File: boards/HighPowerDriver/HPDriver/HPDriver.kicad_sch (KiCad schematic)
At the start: 0 parts

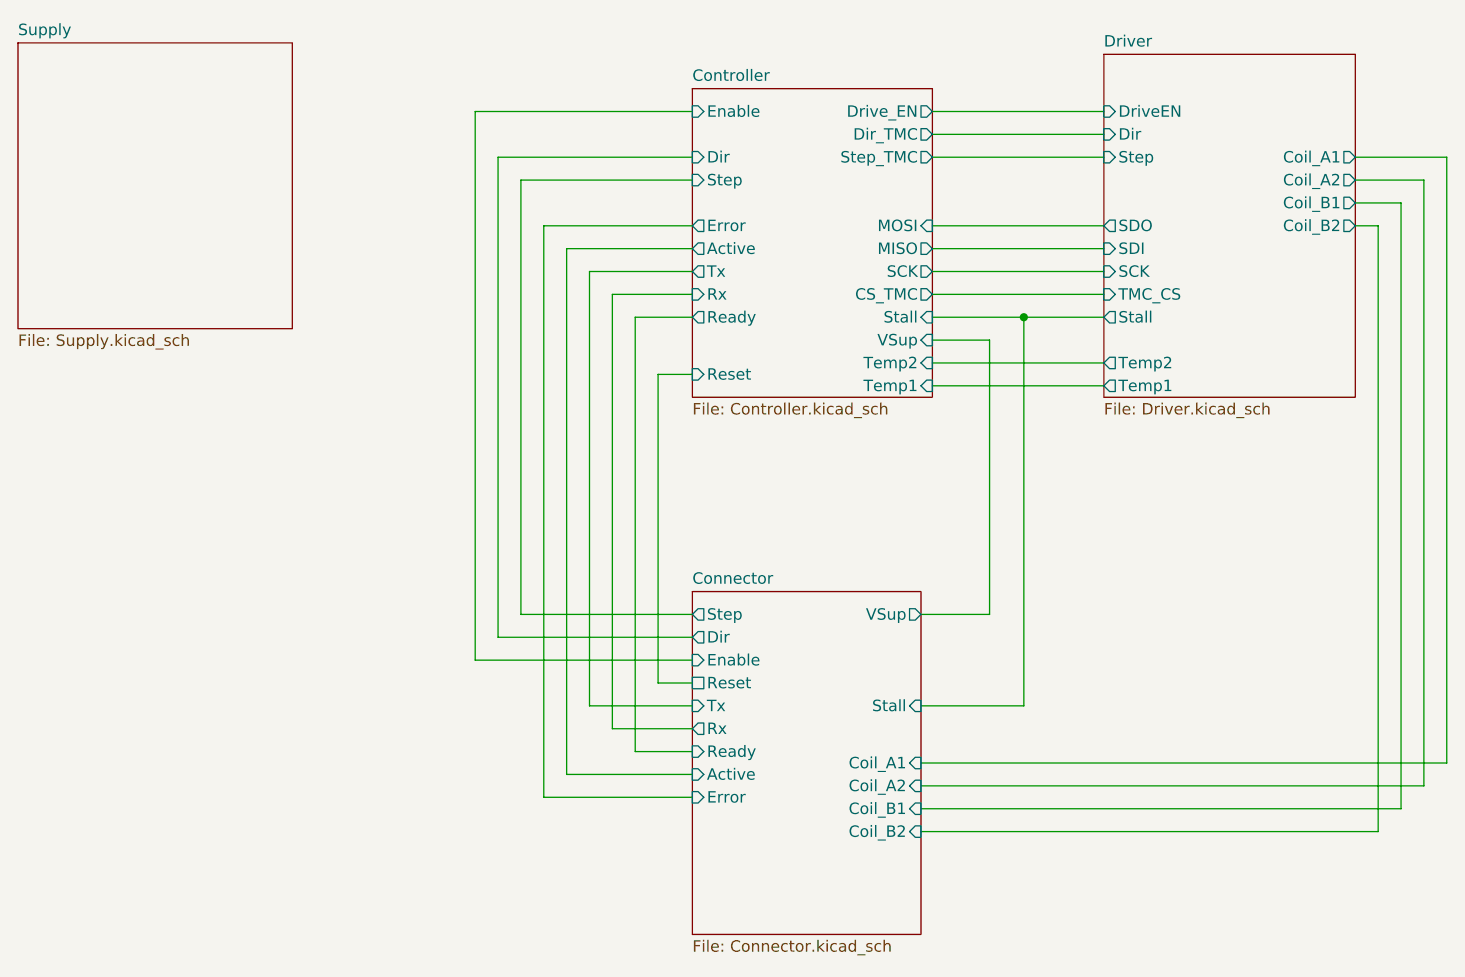
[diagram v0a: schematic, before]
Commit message: Changed Controller to ATmega328PB
The ATtiny did not have enough flash
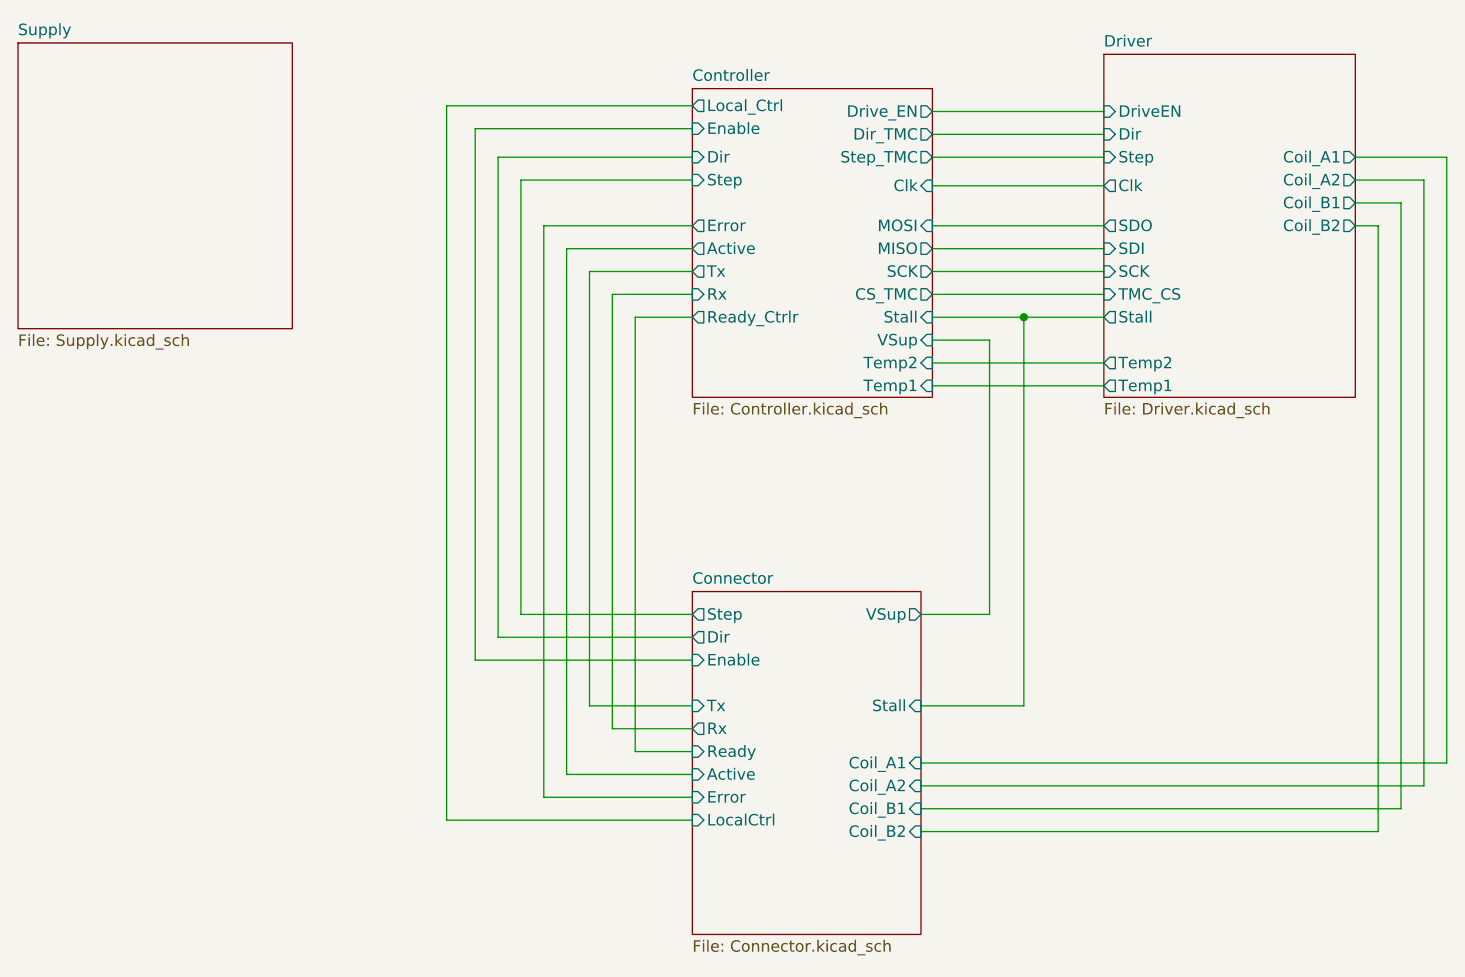
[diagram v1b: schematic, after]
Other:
- sheet Connector ports: added LocalCtrl; removed Reset
- sheet Controller ports: added Clk, Local_Ctrl, Ready_Ctrlr; removed Ready, Reset
- sheet Driver ports: added Clk; removed none
